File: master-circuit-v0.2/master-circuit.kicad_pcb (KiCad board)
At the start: 4 copper layers, 120 x 70 mm, 270 parts, among them U6 20nF 5%, X2 24MHz

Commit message: Almost complete new master circuit schematic.
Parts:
- removed C52, C53: 1uF, Library:C0603
- removed CARD1: ~, Library:TF-SMD_TF-01A
- removed R38, R45, R47, R53, R58, R60, R64: 10kΩ, Library:R0603
- removed R48: 1mΩ, Library:R2725
- removed SCREEN1: ~, Library:FPC-SMD_18P-P0.50_FPC-05F-18PH20
- removed U20: ~, Library:WQFN-16_L3.0-W3.0-P0.50-TL-EP1.7
- removed USB8: ~, Library:USB-C-SMD_TYPE-C16PIN
- added C42: 100nF, Library:C0603, F.Cu at (244.6, -127.0)
- added C43: 100nF, Library:C0603, F.Cu at (239.7, -141.8)
- added C44: 100nF, Library:C0603, F.Cu at (210.0, -119.2)
- added C45: 100nF, Library:C0603, F.Cu at (193.0, -126.5)
- added C46: 1uF, Library:C0603, F.Cu at (74.1, -247.7)
- added C84: 1uF, Library:C0603, F.Cu at (241.0, -129.9)
- added C85: 1uF, Library:C0603, F.Cu at (239.5, -144.3)
- added R79: 100kΩ, Library:R0402, F.Cu at (99.2, -183.7)
- added R80: 100kΩ, Library:R0402, F.Cu at (76.2, -183.2)
- added R82: 100kΩ, Library:R0402, F.Cu at (219.8, -167.2)
- added R83: 100kΩ, Library:R0402, F.Cu at (203.1, -165.1)
- added R84: 100kΩ, Library:R0402, F.Cu at (177.7, -104.2)
- added R91: 100kΩ, Library:R0402, F.Cu at (175.6, -167.4)
- added R92: 100kΩ, Library:R0402, F.Cu at (136.2, -124.5)
- added U35: ~, Library:MSP2807 OLED with touchescreen and SD card, F.Cu at (68.5, 81.5)
- added USB0: ~, Library:USB-C-SMD_TYPE-C16PIN, F.Cu at (40.0, 85.5)
- C14: value 100nF -> 1uF
- R34: value 10kΩ -> 1mΩ; footprint Library:R0603 -> Library:R2725 Shunt with Kelvin connections
- moved U8 355.5 mm to (80.1, -247.8)
- moved Q4 346.7 mm to (78.1, -244.0)
- moved Q3 346.7 mm to (81.9, -245.5)
- moved R19 334.1 mm to (92.9, -247.7), turned to 0 degrees
- moved R34 333.8 mm to (87.8, -256.1)
- moved C37 325.8 mm to (82.4, -247.8)
- moved C36 325.8 mm to (89.5, -247.7)
- moved Q2 325.2 mm to (93.5, -244.0)
- moved Q1 325.2 mm to (97.3, -245.5)
- moved U2 325.2 mm to (95.5, -247.8)
- moved C14 322.1 mm to (97.9, -247.8), turned to 180 degrees
- moved C29 321.4 mm to (116.2, -238.6)
- moved C49 321.4 mm to (107.9, -238.4)
- moved Q5 321.4 mm to (115.7, -236.3)
- moved R36 321.4 mm to (111.3, -238.4)
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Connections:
- C14 pad 2: 3V3 -> /VCC_PROBE
- C36 pad 2: /VCC_PROBE -> VBATTERY
- C37 pad 2: VBATTERY -> /VCC_PROBE
- D4 pad 1: FSPICS0/MEMORY_CS -> FSPIQ/SPI2_MISO
- D4 pad 2: FSPIQ/SPI2_MISO -> FSPICLK/SPI2_CLK
- D6 pad 1: FSPICLK/SPI2_CLK -> FSPICS0/MEMORY_CS
- H2 pad 2: BATTERY_1 -> GPIO1
- H2 pad 3: BATTERY_2 -> GPIO2
- I2C1 pad 3: I2C1_SDA -> I2C_EXTERNAL1_SDA
- I2C1 pad 4: I2C1_SCL -> I2C_EXTERNAL1_SCL
- I2C1 pad 5: unconnected-(I2C1-Pad5) -> GPIO1
- I2C1 pad 6: unconnected-(I2C1-Pad6) -> GPIO2
- I2C2 pad 3: I2C2_SDA -> I2C_EXTERNAL2_SDA
- I2C2 pad 4: I2C2_SCL -> I2C_EXTERNAL2_SCL
- I2C2 pad 5: unconnected-(I2C2-Pad5) -> GPIO1
- I2C2 pad 6: unconnected-(I2C2-Pad6) -> GPIO2
- R11 pad 1: Net-(CARD1-DAT2(RSV)) -> GND
- R11 pad 2: 3V3 -> CONNECT_BATTERY
- R12 pad 1: Net-(CARD1-DAT1(RSV)) -> GND
- R12 pad 2: 3V3 -> CONNECT_VBUS
- R19 pad 1: /CFG_SEL1 -> GND
- R19 pad 2: 3V3 -> CONNECT_BATTERY
- R20 pad 1: 3V3 -> GND
- R20 pad 2: nOCS1 -> CONNECT_BATTERY
- R29 pad 1: 3V3 -> NRESET_ALL_MULTIPLEXERS
- R29 pad 2: nOCS2 -> 3V3
- R30 pad 1: 3V3 -> GND
- R34 pad 1: GND -> /VCC_PROBE
- R34 pad 2: CONNECT_BATTERY -> VCC
- R52 pad 2: Net-(U24-SDA/SMBDATA/NON_REM1) -> /CFG_SEL1
- U1 pad 10: BATTERY_1 -> TOUCH_CS
- U1 pad 12: unconnected-(U1-IO8-Pad12) -> VCC_CURRENT
- U1 pad 15: REFERENCE -> SERVO3_CURRENT
- U1 pad 16: unconnected-(U1-IO46-Pad16) -> CONNECT_VBUS
- U1 pad 17: unconnected-(U1-IO9-Pad17) -> REFERENCE
- U1 pad 22: unconnected-(U1-IO14-Pad22) -> CAN_RX
- U1 pad 23: unconnected-(U1-IO21-Pad23) -> CAN_TX
- U1 pad 24: unconnected-(U1-IO47-Pad24) -> NRESET_ALL_MULTIPLEXERS
- U1 pad 25: BATTERY_2 -> SCREEN_LED
- U1 pad 26: unconnected-(U1-IO45-Pad26) -> CONNECT_BATTERY
- U1 pad 38: CAN_RX -> SERVO2_CURRENT
- U1 pad 39: CAN_TX -> SERVO1_CURRENT
- U1 pad 4: VBUS_VOLTAGE -> SERVO4_CURRENT
- U1 pad 5: VCC_CURRENT -> SERVO5_CURRENT
- U1 pad 6: CONNECT_VBUS -> SERVO6_CURRENT
- U1 pad 7: CONNECT_BATTERY -> SERVO7_CURRENT
- U1 pad 8: unconnected-(U1-IO15-Pad8) -> VBUS_VOLTAGE
- U13 pad 1: unconnected-(U13-A0-Pad1) -> 3V3
- U13 pad 17: unconnected-(U13-SD6-Pad17) -> I2C_EXTERNAL1_SDA
- U13 pad 18: unconnected-(U13-SC6-Pad18) -> I2C_EXTERNAL1_SCL
- U13 pad 19: unconnected-(U13-SD7-Pad19) -> I2C_EXTERNAL2_SDA
- U13 pad 2: unconnected-(U13-A1-Pad2) -> 3V3
- U13 pad 20: unconnected-(U13-SC7-Pad20) -> I2C_EXTERNAL2_SCL
- U13 pad 21: unconnected-(U13-A2-Pad21) -> 3V3
- U13 pad 22: unconnected-(U13-SCL-Pad22) -> I2C2_SCL
- U13 pad 23: unconnected-(U13-SDA-Pad23) -> I2C2_SDA
- U13 pad 24: unconnected-(U13-VCC-Pad24) -> 3V3
- U13 pad 3: unconnected-(U13-RESET#-Pad3) -> NRESET_ALL_MULTIPLEXERS
- U14 pad 1: unconnected-(U14-SCL-Pad1) -> I2C1_SCL
- U14 pad 15: unconnected-(U14-RESET#-Pad15) -> NRESET_ALL_MULTIPLEXERS
- U14 pad 16: unconnected-(U14-VDD-Pad16) -> 3V3
- U14 pad 2: unconnected-(U14-SDA-Pad2) -> I2C1_SDA
- U14 pad 3: unconnected-(U14-A0-Pad3) -> GND
- U14 pad 4: unconnected-(U14-A1-Pad4) -> GND
- U14 pad 5: unconnected-(U14-A2-Pad5) -> GND
- U15 pad 1: unconnected-(U15-SCL-Pad1) -> I2C1_SCL
- U15 pad 13: unconnected-(U15-IO6-Pad13) -> GPIO1
- U15 pad 14: unconnected-(U15-IO7-Pad14) -> GPIO2
- U15 pad 15: unconnected-(U15-RESET#-Pad15) -> NRESET_ALL_MULTIPLEXERS
- U15 pad 16: unconnected-(U15-VDD-Pad16) -> 3V3
- U15 pad 2: unconnected-(U15-SDA-Pad2) -> I2C1_SDA
- U15 pad 3: unconnected-(U15-A0-Pad3) -> 3V3
- U15 pad 4: unconnected-(U15-A1-Pad4) -> GND
- U15 pad 5: unconnected-(U15-A2-Pad5) -> GND
- U18 pad 4: I2C2_SDA -> I2C1_SDA
- U18 pad 6: I2C2_SCL -> I2C1_SCL
- U24 pad 40: Net-(U24-SDA/SMBDATA/NON_REM1) -> I2C1_SDA
- U24 pad 41: /CFG_SEL0 -> I2C1_SCL
- U24 pad 43: NRESET_USB_HUB -> NRESET_ALL_MULTIPLEXERS
- U24 pad 58: unconnected-(U24-USBUP_DM-Pad58) -> INTERNAL_GUEST_USB_D-
- U24 pad 59: unconnected-(U24-USBUP_DP-Pad59) -> INTERNAL_GUEST_USB_D+
- U9 pad 1: unconnected-(U9-A0-Pad1) -> GND
- U9 pad 2: unconnected-(U9-A1-Pad2) -> GND
- U9 pad 21: unconnected-(U9-A2-Pad21) -> GND
- U9 pad 22: unconnected-(U9-SCL-Pad22) -> I2C1_SCL
- U9 pad 23: unconnected-(U9-SDA-Pad23) -> I2C1_SDA
- U9 pad 24: unconnected-(U9-VCC-Pad24) -> 3V3
- U9 pad 3: unconnected-(U9-RESET#-Pad3) -> NRESET_ALL_MULTIPLEXERS
- USB2 pad 1: unconnected-(USB2-SHELL-Pad1) -> GND
- USB2 pad 2: unconnected-(USB2-SHELL-Pad2) -> GND
- USB2 pad 3: unconnected-(USB2-SHELL-Pad3) -> GND
- USB2 pad 4: unconnected-(USB2-SHELL-Pad4) -> GND
- USB2 pad A4B9: VBUS -> /servo-usb-connector6/VBUSx
- USB2 pad A5: CC1 -> /servo-usb-connector6/CC1x
- USB2 pad A6: GUEST_USB_D+ -> USBDN7_D+
- USB2 pad A7: GUEST_USB_D- -> USBDN7_D-
- USB2 pad A8: ENABLE-ESP32 -> SERVO7_BOOT0
- USB2 pad B4A9: VBUS -> /servo-usb-connector6/VBUSx
- USB2 pad B5: CC2 -> /servo-usb-connector6/CC2x
- USB2 pad B6: GUEST_USB_D+ -> USBDN7_D+
- USB2 pad B7: GUEST_USB_D- -> USBDN7_D-
- USB2 pad B8: BOOT0 -> SERVO7_NRST

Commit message: Drop unused features and arrange components on new master circuit board.
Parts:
- removed C41, C82, C83: 1uF, Library:C0603
- removed D12: ~, Library:SOT-23-3_L3.0-W1.7-P0.95-LS2.9-BR
- removed FPC7: ~, Library:FPC-SMD_20P-P0.50_XUNPU_FPC-05F-20PH20
- removed H1, H2: ~, Library:HDR-TH_4P-P2.54-V-M
- removed I2C1, I2C2: ~, Library:FPC-SMD_6P-P0.50_XUNPU_FPC-05F-6PH20
- removed Q21, Q22: ~, Library:WDFN-5_L3.1-W3.1-P0.65-BL_1
- removed R102, R109: 1MΩ, Library:R0402
- removed R68, R73, R74, R78: 5mΩ, Library:R2512 Shunt with Kelvin connections
- removed R72: 20kΩ, Library:R0402
- removed R77, R90: 56kΩ, Library:R0603
- removed R81: 10kΩ, Library:R0603
- removed R92: 100kΩ, Library:R0402
- removed REF** (x4): NPTH 2mm hole 3mm clearence, Library:NPTH 2mm hole 3mm clearence
- removed U33: ~, Library:WLCSP-6_L1.2-W0.8-P0.40-TL
- removed U34: ~, Library:SOT-23-6_L2.9-W1.6-P0.95-LS2.8-BR
- removed USB7: ~, Library:USB-C-SMD_TYPE-C16PIN
- added R38: 10kΩ, Library:R0603, F.Cu at (120.7, 86.6)
- added R45: 100kΩ, Library:R0603, F.Cu at (117.7, 86.6)
- added R47: 10kΩ, Library:R0603, F.Cu at (116.2, 86.6)
- added R48: 100kΩ, Library:R0603, F.Cu at (119.2, 86.6)
- added R53: 10kΩ, Library:R0603, F.Cu at (195.4, 62.4)
- added R58: 10kΩ, Library:R0603, F.Cu at (201.9, 62.6)
- added R60: 10kΩ, Library:R0603, F.Cu at (146.0, 128.1)
- added R64: 10kΩ, Library:R0603, F.Cu at (145.9, 126.6)
- C12, C13, C14, C20, C21, C22, C23, C24, C29, C34, C35, C36, C37, C38, C39, C46, C49, C57, C58, C6, C7, C72, C73, C74, C75, C76, C77, C78, C79, C8, C80, C81, C9, D13, D3, D8, FPC1, FPC2, FPC3, FPC4, FPC5, FPC6, L1, L2, Q1, Q10, Q11, Q12, Q13, Q14, Q15, Q16, Q17, Q18, Q19, Q2, Q20, Q3, Q4, Q5, Q6, Q7, Q8, Q9, R10, R19, R20, R21, R22, R36, R43, R44, R49, R54, R57, R63, R69, R75, R84, U11, U12, U16, U2, U21, U22, U25, U27, U29, U3, U31, U4, U8, USB0: moved to B.Cu
- R1, R3, R7: value 10kΩ -> 5mΩ; footprint Library:R0603 -> Library:R2512 Shunt with Kelvin connections; moved to B.Cu
- R2, R4, R5: value 100kΩ -> 5mΩ; footprint Library:R0603 -> Library:R2512 Shunt with Kelvin connections; moved to B.Cu
- R34: value 1mΩ -> 10kΩ; footprint Library:R2725 Shunt with Kelvin connections -> Library:R0603
- R37: value 5mΩ -> 10kΩ; footprint Library:R2512 Shunt with Kelvin connections -> Library:R0603
- R56: value 5mΩ -> 100kΩ; footprint Library:R2512 Shunt with Kelvin connections -> Library:R0603; moved to B.Cu
- R6: value 13kΩ -> 5mΩ; footprint Library:R0603 -> Library:R2512 Shunt with Kelvin connections; moved to B.Cu
- R62: value 5mΩ -> 13kΩ; footprint Library:R2512 Shunt with Kelvin connections -> Library:R0603; moved to B.Cu
- R8: value 10kΩ -> 1mΩ; footprint Library:R0603 -> Library:R2725 Shunt with Kelvin connections; moved to B.Cu
- moved C37 366.6 mm to (122.3, 116.6), turned to 90 degrees
- moved C14 365.1 mm to (115.5, 116.8), turned to 90 degrees
- moved U8 364.5 mm to (122.3, 114.3), turned to 90 degrees
- moved Q3 364.2 mm to (124.6, 116.1), turned to 90 degrees
- moved U2 362.8 mm to (115.6, 114.5), turned to 90 degrees
- moved Q1 362.4 mm to (117.8, 116.3), turned to 90 degrees
- moved R20 362.2 mm to (122.4, 111.7), turned to -90 degrees
- moved R19 360.2 mm to (115.7, 111.9), turned to -90 degrees
- moved Q4 359.5 mm to (126.1, 112.3), turned to -90 degrees
- moved C46 359.2 mm to (122.4, 108.3), turned to 90 degrees
- moved Q2 357.4 mm to (119.3, 112.5), turned to -90 degrees
- moved C36 357.1 mm to (115.7, 108.5), turned to 90 degrees
- moved C29 342.0 mm to (116.8, 103.5), turned to 90 degrees
- moved U12 339.6 mm to (116.8, 101.1), turned to 90 degrees
- moved Q5 339.2 mm to (119.1, 102.9), turned to 90 degrees
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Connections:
- net Net-(U24-RBIAS) renamed /RBIAS
- C14 pad 2: /VCC_PROBE -> /VBATTERY_PROBE
- C29 pad 2: /VCC_PROBE -> /VBUS_PROBE
- C37 pad 2: /VCC_PROBE -> /VBATTERY_PROBE
- Q1 pad 1: /VCC_PROBE -> /VBATTERY_PROBE
- Q1 pad 2: /VCC_PROBE -> /VBATTERY_PROBE
- Q1 pad 3: /VCC_PROBE -> /VBATTERY_PROBE
- Q3 pad 1: /VCC_PROBE -> /VBATTERY_PROBE
- Q3 pad 2: /VCC_PROBE -> /VBATTERY_PROBE
- Q3 pad 3: /VCC_PROBE -> /VBATTERY_PROBE
- Q5 pad 1: /VCC_PROBE -> /VBUS_PROBE
- Q5 pad 2: /VCC_PROBE -> /VBUS_PROBE
- Q5 pad 3: /VCC_PROBE -> /VBUS_PROBE
- R1 pad 1: ENABLE-ESP32 -> /servo-usb-connector/back-to-back-mosfets3/VIN
- R1 pad 2: 3V3 -> VCC
- R2 pad 1: VBUS_VOLTAGE -> /servo-usb-connector1/back-to-back-mosfets3/VIN
- R2 pad 2: VBUS -> VCC
- R3 pad 1: GND -> /servo-usb-connector2/back-to-back-mosfets3/VIN
- R3 pad 2: VBUS_VOLTAGE -> VCC
- R34 pad 1: /VCC_PROBE -> FSPID/SPI2_MOSI
- R34 pad 2: VCC -> 3V3
- R37 pad 1: /servo-usb-connector/back-to-back-mosfets3/VIN -> ENABLE-ESP32
- R37 pad 2: VCC -> 3V3
- R4 pad 1: BATTERY_VOLTAGE -> /servo-usb-connector3/back-to-back-mosfets3/VIN
- R4 pad 2: VBATTERY -> VCC
- R5 pad 1: Buck-FB -> /servo-usb-connector4/back-to-back-mosfets3/VIN
- R5 pad 2: /Buck-Probe-Point -> VCC
- R56 pad 1: /servo-usb-connector1/back-to-back-mosfets3/VIN -> Buck-FB
- R56 pad 2: VCC -> /Buck-Probe-Point
- R6 pad 1: GND -> /servo-usb-connector5/back-to-back-mosfets3/VIN
- R6 pad 2: Buck-FB -> VCC
- R62 pad 1: /servo-usb-connector2/back-to-back-mosfets3/VIN -> GND
- R62 pad 2: VCC -> Buck-FB
- R7 pad 1: GND -> /VBUS_PROBE
- R7 pad 2: BATTERY_VOLTAGE -> VCC
- R8 pad 1: FSPID/SPI2_MOSI -> /VBATTERY_PROBE
- R8 pad 2: 3V3 -> VCC
- U12 pad C1: /VCC_PROBE -> /VBUS_PROBE
- U13 pad 10: SERVO6_NRST -> SERVO5_NRST
- U13 pad 11: SERVO6_BOOT0 -> SERVO5_BOOT0
- U13 pad 13: SERVO7_BOOT0 -> SERVO6_BOOT0
- U13 pad 14: SERVO7_NRST -> SERVO6_NRST
- U13 pad 15: SERVO7_NRST -> SERVO6_NRST
- U13 pad 16: SERVO7_BOOT0 -> SERVO6_BOOT0
- U13 pad 17: I2C_EXTERNAL1_SDA -> unconnected-(U13-SD6-Pad17)
- U13 pad 18: I2C_EXTERNAL1_SCL -> unconnected-(U13-SC6-Pad18)
- U13 pad 19: I2C_EXTERNAL2_SDA -> I2C2_INTERNAL_SCL
- U13 pad 20: I2C_EXTERNAL2_SCL -> I2C2_INTERNAL_SDA
- U13 pad 4: SERVO5_BOOT0 -> SERVO4_BOOT0
- U13 pad 5: SERVO5_NRST -> SERVO4_NRST
- U13 pad 6: SERVO5_NRST -> SERVO4_NRST
- U13 pad 7: SERVO5_BOOT0 -> SERVO4_BOOT0
- U13 pad 8: SERVO6_BOOT0 -> SERVO5_BOOT0
- U13 pad 9: SERVO6_NRST -> SERVO5_NRST
- U14 pad 1: I2C1_SCL -> I2C1_INTERNAL_SCL
- U14 pad 13: SERVO4_BOOT0 -> unconnected-(U14-IO6-Pad13)
- U14 pad 14: SERVO4_NRST -> unconnected-(U14-IO7-Pad14)
- U14 pad 2: I2C1_SDA -> I2C1_INTERNAL_SDA
- U15 pad 1: I2C1_SCL -> I2C2_INTERNAL_SCL
- U15 pad 10: SERVO6_NRST -> SERVO5_NRST
- U15 pad 11: SERVO7_BOOT0 -> SERVO6_BOOT0
- U15 pad 12: SERVO7_NRST -> SERVO6_NRST
- U15 pad 13: GPIO1 -> unconnected-(U15-IO6-Pad13)
- U15 pad 14: GPIO2 -> unconnected-(U15-IO7-Pad14)
- U15 pad 2: I2C1_SDA -> I2C2_INTERNAL_SDA
- U15 pad 3: 3V3 -> GND
- U15 pad 6: SERVO5_BOOT0 -> SERVO4_BOOT0
- U15 pad 7: SERVO5_NRST -> SERVO4_NRST
- U15 pad 9: SERVO6_BOOT0 -> SERVO5_BOOT0
- U18 pad 4: I2C1_SDA -> I2C2_INTERNAL_SDA
- U18 pad 6: I2C1_SCL -> I2C2_INTERNAL_SCL
- U2 pad C1: /VCC_PROBE -> /VBATTERY_PROBE
- U24 pad 36: PRTPWR7 -> unconnected-(U24-PRTPWR7-Pad36)
- U24 pad 37: nOCS7 -> 3V3
- U24 pad 40: I2C1_SDA -> I2C1_INTERNAL_SCL
- U24 pad 41: I2C1_SCL -> I2C1_INTERNAL_SDA
- U24 pad 55: USBDN7_D- -> GND
- U24 pad 56: USBDN7_D+ -> GND
- U8 pad C1: /VCC_PROBE -> /VBATTERY_PROBE
- U9 pad 1: GND -> 3V3
- U9 pad 17: SERVO4_BOOT0 -> unconnected-(U9-SD6-Pad17)
- U9 pad 18: SERVO4_NRST -> unconnected-(U9-SC6-Pad18)
- U9 pad 19: SERVO4_NRST -> I2C1_INTERNAL_SCL
- U9 pad 2: GND -> 3V3
- U9 pad 20: SERVO4_BOOT0 -> I2C1_INTERNAL_SDA
- U9 pad 21: GND -> 3V3
- USB2 pad A4B9: /servo-usb-connector6/VBUSx -> /servo-usb-connector1/VBUSx
- USB2 pad A5: /servo-usb-connector6/CC1x -> /servo-usb-connector1/CC1x
- USB2 pad A6: USBDN7_D+ -> USBDN2_D+
- USB2 pad A7: USBDN7_D- -> USBDN2_D-
- USB2 pad A8: SERVO7_BOOT0 -> SERVO2_BOOT0
- USB2 pad B4A9: /servo-usb-connector6/VBUSx -> /servo-usb-connector1/VBUSx
- USB2 pad B5: /servo-usb-connector6/CC2x -> /servo-usb-connector1/CC2x
- USB2 pad B6: USBDN7_D+ -> USBDN2_D+
- USB2 pad B7: USBDN7_D- -> USBDN2_D-
- USB2 pad B8: SERVO7_NRST -> SERVO2_NRST
- USB3 pad A4B9: /servo-usb-connector1/VBUSx -> /servo-usb-connector2/VBUSx
- USB3 pad A5: /servo-usb-connector1/CC1x -> /servo-usb-connector2/CC1x
- USB3 pad A6: USBDN2_D+ -> USBDN3_D+
- USB3 pad A7: USBDN2_D- -> USBDN3_D-
- USB3 pad A8: SERVO2_BOOT0 -> SERVO3_BOOT0
- USB3 pad B4A9: /servo-usb-connector1/VBUSx -> /servo-usb-connector2/VBUSx
- USB3 pad B5: /servo-usb-connector1/CC2x -> /servo-usb-connector2/CC2x
- USB3 pad B6: USBDN2_D+ -> USBDN3_D+
- USB3 pad B7: USBDN2_D- -> USBDN3_D-
- USB3 pad B8: SERVO2_NRST -> SERVO3_NRST
- USB4 pad A4B9: /servo-usb-connector2/VBUSx -> /servo-usb-connector3/VBUSx
- USB4 pad A5: /servo-usb-connector2/CC1x -> /servo-usb-connector3/CC1x
- USB4 pad A6: USBDN3_D+ -> USBDN4_D+
- USB4 pad A7: USBDN3_D- -> USBDN4_D-
- USB4 pad A8: SERVO3_BOOT0 -> SERVO4_BOOT0
- USB4 pad B4A9: /servo-usb-connector2/VBUSx -> /servo-usb-connector3/VBUSx
- USB4 pad B5: /servo-usb-connector2/CC2x -> /servo-usb-connector3/CC2x
- USB4 pad B6: USBDN3_D+ -> USBDN4_D+
- USB4 pad B7: USBDN3_D- -> USBDN4_D-
- USB4 pad B8: SERVO3_NRST -> SERVO4_NRST
- USB5 pad A4B9: /servo-usb-connector3/VBUSx -> /servo-usb-connector4/VBUSx
- USB5 pad A5: /servo-usb-connector3/CC1x -> /servo-usb-connector4/CC1x
- USB5 pad A6: USBDN4_D+ -> USBDN5_D+
- USB5 pad A7: USBDN4_D- -> USBDN5_D-
- USB5 pad A8: SERVO4_BOOT0 -> SERVO5_BOOT0
- USB5 pad B4A9: /servo-usb-connector3/VBUSx -> /servo-usb-connector4/VBUSx
- USB5 pad B5: /servo-usb-connector3/CC2x -> /servo-usb-connector4/CC2x
- USB5 pad B6: USBDN4_D+ -> USBDN5_D+
- USB5 pad B7: USBDN4_D- -> USBDN5_D-
- USB5 pad B8: SERVO4_NRST -> SERVO5_NRST
- USB6 pad A4B9: /servo-usb-connector4/VBUSx -> /servo-usb-connector5/VBUSx
- USB6 pad A5: /servo-usb-connector4/CC1x -> /servo-usb-connector5/CC1x
- USB6 pad A6: USBDN5_D+ -> USBDN6_D+
- USB6 pad A7: USBDN5_D- -> USBDN6_D-
- USB6 pad A8: SERVO5_BOOT0 -> SERVO6_BOOT0
- USB6 pad B4A9: /servo-usb-connector4/VBUSx -> /servo-usb-connector5/VBUSx
- USB6 pad B5: /servo-usb-connector4/CC2x -> /servo-usb-connector5/CC2x
- USB6 pad B6: USBDN5_D+ -> USBDN6_D+
- USB6 pad B7: USBDN5_D- -> USBDN6_D-
- USB6 pad B8: SERVO5_NRST -> SERVO6_NRST
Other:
- board size 120 x 70 mm -> 69 x 86 mm
- board text added: "Guest USB"
- board text added: "Touch Screen"
- board text removed: "< CAN"
- board text removed: "< USB to Host"
- board text removed: "B0 RST SCL SDA 3V3 GND"
- board text removed: "GND BAT2 BAT1 VBAT"
- board text removed: "I2C1"
- board text removed: "I2C2"
- board text removed: "IMU Position"
- board text removed: "IMU is 50mm from edge below"
- board text removed: "Plugin Touch Screen"
- board text removed: "RX TX 3V3 GND"
- board text removed: "USB to Sensor"

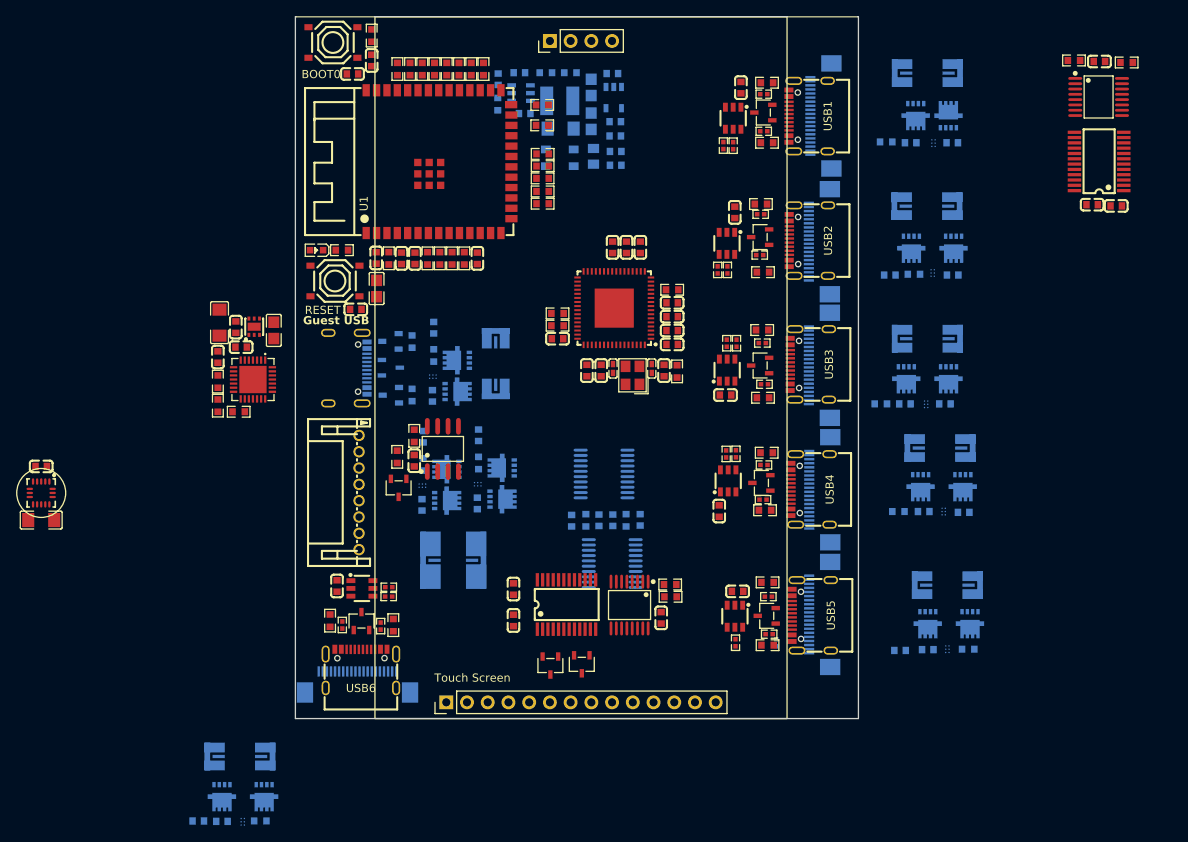
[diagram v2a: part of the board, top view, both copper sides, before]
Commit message: Connect one of the USB outputs, outline part placement.
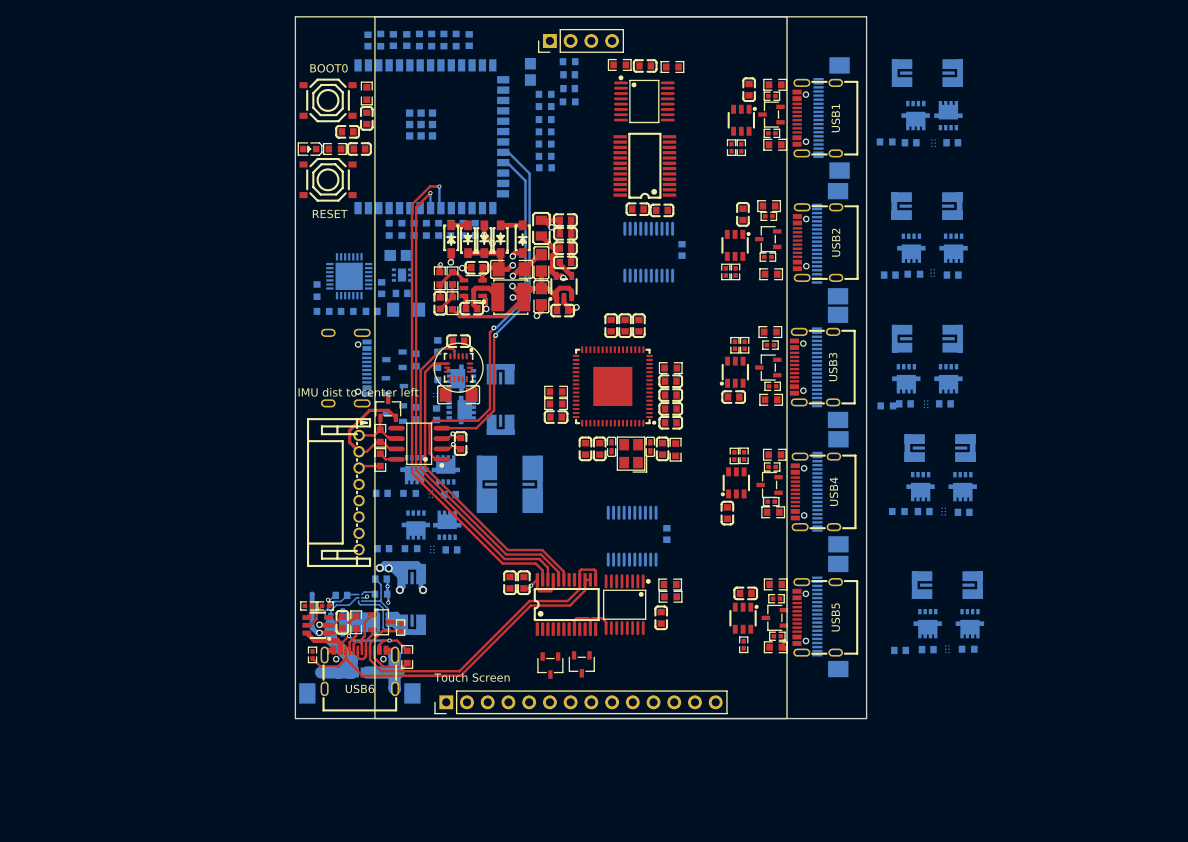
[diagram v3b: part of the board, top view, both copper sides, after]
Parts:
- added D12: ~, Library:SOD-123_L2.7-W1.6-LS3.7-RD-1, F.Cu at (119.1, 84.2)
- added D14: ~, Library:SOD-123_L2.7-W1.6-LS3.7-RD-1, F.Cu at (127.8, 84.2)
- added D15: ~, Library:SOD-123_L2.7-W1.6-LS3.7-RD-1, F.Cu at (123.2, 84.2)
- C1, C10, C11, C16, C17, C18, C19, C2, C3, R11, R12, R14, R15, R17, R18, R24, R25, R26, R27, R29, R32, R33, R34, R37, R38, R39, R40, R41, R45, R47, R48, R9, U1, U10, U5, U6: moved to B.Cu
- C12, C13, C20, C21, C22, C23, C24, C6, C7, C8, C9, D13, D3, L1, L2, R10, R56, R62, U3, U4: moved to F.Cu
- moved R22 56.2 mm to (133.6, 62.5), turned to 180 degrees
- moved C42 55.7 mm to (142.0, 80.6)
- moved R53 55.7 mm to (139.8, 62.9)
- moved R58 55.7 mm to (146.2, 63.1)
- moved U14 55.7 mm to (142.8, 67.4)
- moved U9 55.7 mm to (142.8, 75.3)
- moved C45 55.7 mm to (142.9, 63.0)
- moved C84 55.7 mm to (144.9, 80.7)
- moved C35 54.7 mm to (133.6, 64.1), turned to 180 degrees
- moved C31 53.4 mm to (120.0, 96.8)
- moved C32 53.4 mm to (120.0, 103.3)
- moved U18 53.4 mm to (120.0, 100.0)
- moved C34 53.2 mm to (133.6, 65.8), turned to 180 degrees
- moved R21 51.8 mm to (133.6, 67.4), turned to 0 degrees
- moved C81 37.2 mm to (110.5, 125.9), turned to 180 degrees
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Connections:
- net Net-(Q1-D) renamed /back-to-back-mosfets1/Mid-MOSFETSx
- net Net-(Q1-G) renamed /back-to-back-mosfets1/GATE2x
- net Net-(Q11-D) renamed /servo-usb-connector1/back-to-back-mosfets3/Mid-MOSFETSx
- net Net-(Q11-G) renamed /servo-usb-connector1/back-to-back-mosfets3/GATE2x
- net Net-(Q12-G) renamed /servo-usb-connector1/back-to-back-mosfets3/GATE1x
- net Net-(Q13-D) renamed /servo-usb-connector2/back-to-back-mosfets3/Mid-MOSFETSx
- net Net-(Q13-G) renamed /servo-usb-connector2/back-to-back-mosfets3/GATE2x
- net Net-(Q14-G) renamed /servo-usb-connector2/back-to-back-mosfets3/GATE1x
- net Net-(Q15-D) renamed /servo-usb-connector3/back-to-back-mosfets3/Mid-MOSFETSx
- net Net-(Q15-G) renamed /servo-usb-connector3/back-to-back-mosfets3/GATE2x
- net Net-(Q16-G) renamed /servo-usb-connector3/back-to-back-mosfets3/GATE1x
- net Net-(Q17-D) renamed /servo-usb-connector4/back-to-back-mosfets3/Mid-MOSFETSx
- net Net-(Q17-G) renamed /servo-usb-connector4/back-to-back-mosfets3/GATE2x
- net Net-(Q18-G) renamed /servo-usb-connector4/back-to-back-mosfets3/GATE1x
- net Net-(Q19-D) renamed /servo-usb-connector5/back-to-back-mosfets3/Mid-MOSFETSx
- net Net-(Q19-G) renamed /servo-usb-connector5/back-to-back-mosfets3/GATE2x
- net Net-(Q2-G) renamed /back-to-back-mosfets1/GATE1x
- net Net-(Q20-G) renamed /servo-usb-connector5/back-to-back-mosfets3/GATE1x
- net Net-(Q3-D) renamed /back-to-back-mosfets2/Mid-MOSFETSx
- net Net-(Q3-G) renamed /back-to-back-mosfets2/GATE2x
- net Net-(Q4-G) renamed /back-to-back-mosfets2/GATE1x
- net Net-(Q5-D) renamed /back-to-back-mosfets/Mid-MOSFETSx
- net Net-(Q5-G) renamed /back-to-back-mosfets/GATE2x
- net Net-(Q6-G) renamed /back-to-back-mosfets/GATE1x
- net Net-(Q7-D) renamed /servo-usb-connector/back-to-back-mosfets3/Mid-MOSFETSx
- net Net-(Q7-G) renamed /servo-usb-connector/back-to-back-mosfets3/GATE2x
- net Net-(Q8-G) renamed /servo-usb-connector/back-to-back-mosfets3/GATE1x
- net Net-(U17-RS) renamed /CAN-RS-SLOPE_CONTROL
- C21 pad 2: VCC -> /Buck-VIN
- C22 pad 2: VCC -> /Buck-VIN
- D13 pad 1: VCC -> /Buck-VIN
- D13 pad 2: VBUS -> /VBUS_MID_DIODE
- D3 pad 1: VCC -> /Buck-VIN
- D3 pad 2: VBATTERY -> /VBATTERY_MID_DIODE
- U4 pad 3: VCC -> /Buck-VIN
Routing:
- net I2C2_SDA: track 0.00 -> 62.0 mm, vias 0 -> 1
- net I2C2_SCL: track 0.00 -> 59.2 mm, vias 0 -> 1
- net CAN_TX: track 0.00 -> 47.1 mm, vias 0 -> 1
- net GND: track 0.00 -> 44.6 mm, vias 0 -> 15
- net CAN_RX: track 0.00 -> 42.5 mm, vias 0 -> 1
- net SERVO6_NRST: track 0.00 -> 42.4 mm
- net SERVO6_BOOT0: track 0.00 -> 42.2 mm
- net I2C2_INTERNAL_SDA: track 0.00 -> 41.2 mm
- net I2C2_INTERNAL_SCL: track 0.00 -> 38.1 mm
- net 5V: track 0.00 -> 34.1 mm, vias 0 -> 3
- net /servo-usb-connector5/back-to-back-mosfets3/VIN: track 0.00 -> 22.0 mm
- net /servo-usb-connector5/VCCx: track 0.00 -> 20.9 mm
- net /servo-usb-connector5/VBUSx: track 0.00 -> 20.4 mm, vias 0 -> 2
- net VCC: track 0.00 -> 19.7 mm, vias 0 -> 6
- net 3V3: track 0.00 -> 17.1 mm, vias 0 -> 3
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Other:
- board size 69 x 86 mm -> 70 x 86 mm
- board text added: "IMU dist to center left"
- board text added: "USB in"
- board text removed: "Guest USB"

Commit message: Design block experimentation.
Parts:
- R84: moved to F.Cu
- moved R69 28.7 mm to (154.4, 128.3), turned to -90 degrees
- moved C76 27.3 mm to (154.6, 117.7), turned to 90 degrees
- moved C72 26.0 mm to (154.6, 86.8), turned to 90 degrees
- moved C57 25.9 mm to (154.6, 71.3), turned to 90 degrees
- moved U29 25.3 mm to (154.9, 130.9), turned to 90 degrees
- moved C74 25.1 mm to (154.6, 102.2), turned to 90 degrees
- moved Q18 24.9 mm to (157.9, 128.2)
- moved R5 24.9 mm to (155.1, 124.5), turned to 180 degrees
- moved C77 24.9 mm to (152.6, 112.8), turned to -90 degrees
- moved U27 24.6 mm to (154.9, 115.4), turned to 90 degrees
- moved Q16 23.9 mm to (157.9, 112.7)
- moved R4 23.9 mm to (155.1, 109.0)
- moved C58 23.6 mm to (152.6, 66.5), turned to -90 degrees
- moved U21 23.5 mm to (154.9, 69.0), turned to 90 degrees
- moved U22 23.5 mm to (154.9, 84.5), turned to 90 degrees
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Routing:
- net GND: track 44.6 -> 169.1 mm, vias 15 -> 54
- net VCC: track 19.7 -> 141.4 mm, vias 6 -> 34
- net 5V: track 34.1 -> 75.9 mm, vias 3 -> 8
- net VBATTERY: track 1.17 -> 38.9 mm
- net VBUS: track 1.45 -> 34.9 mm, vias 1 -> 5
- net /VBATTERY_PROBE: track 0.00 -> 30.3 mm
- net /servo-usb-connector/back-to-back-mosfets3/VIN: track 0.00 -> 22.0 mm
- net /servo-usb-connector3/back-to-back-mosfets3/VIN: track 0.00 -> 22.0 mm
- net /servo-usb-connector1/back-to-back-mosfets3/VIN: track 0.00 -> 22.0 mm
- net /servo-usb-connector4/back-to-back-mosfets3/VIN: track 0.00 -> 22.0 mm
- net /servo-usb-connector2/back-to-back-mosfets3/VIN: track 0.00 -> 22.0 mm
- net /servo-usb-connector4/VCCx: track 0.00 -> 20.9 mm
- net /servo-usb-connector3/VCCx: track 0.00 -> 20.9 mm
- net /servo-usb-connector1/VCCx: track 0.00 -> 20.9 mm
- net /servo-usb-connector/VCCx: track 0.00 -> 20.9 mm
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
